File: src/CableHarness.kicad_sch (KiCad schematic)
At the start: 11 parts

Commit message: Update Schematics design
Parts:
- removed J?: MiniFit_2x10_M, Connector_Molex:Molex_Mini-Fit_Jr_5566-20A_2x10_P4.20mm_Vertical, symbol Connector_Generic:Conn_02x10_Counter_Clockwise
- removed J?: MiniFit_2x04_M, Connector_Molex:Molex_Mini-Fit_Jr_5566-08A_2x04_P4.20mm_Vertical, symbol Connector_Generic:Conn_02x04_Counter_Clockwise
- added J13: MiniFit_2x09_F, Connector_Molex:Molex_Mini-Fit_Jr_5566-18A_2x09_P4.20mm_Vertical, symbol Connector_Generic:Conn_02x09_Counter_Clockwise
- added J?: MiniFit_2x05_M, Connector_Molex:Molex_Mini-Fit_Jr_5566-10A_2x05_P4.20mm_Vertical, symbol Connector_Generic:Conn_02x05_Counter_Clockwise
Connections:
- net +5V: now also J13.5 (Pin_5)
- net +BATT: now also J13.1 (Pin_1)
- net ABeam1: now also J13.13 (Pin_13)
- net ABeam2: now also J13.11 (Pin_11)
- net Accessory: now also J?.10 (Pin_10)
- net AuxSwitch1: now also J13.12 (Pin_12)
- net AuxSwitch2: now also J13.10 (Pin_10)
- net BSignal: now also J?.4 (Pin_4)
- net EBlinker: now also J13.6 (Pin_6), J?.5 (Pin_5)
- net GND: no longer J?.4 (Pin_4)
- net HBeam: now also J?.9 (Pin_9)
- net Key: now also J13.7 (Pin_7), J?.1 (Pin_1)
- net Killswitch: now also J13.8 (Pin_8)
- net LBeam: now also J?.8 (Pin_8)
- net LBlinker: now also J?.3 (Pin_3)
- net LowBat: now also J13.9 (Pin_9)
- net PLight: now also J13.14 (Pin_14), J?.7 (Pin_7)
- net RBlinker: now also J?.2 (Pin_2)
- net VInst: now also J13.4 (Pin_4)
- net VLight: now also J13.2 (Pin_2)
- net VRadio: now also J13.3 (Pin_3)
- net GND1 renamed GNDDash
- net GNDDash: now also J13.18 (Pin_18)
- net GND2 renamed GNDEBlinker
- net GNDEBlinker: now also J13.17 (Pin_17)
- net LightSensor: no longer names the net of J?.3 (Pin_3)
- new net GNDRadio: J13.16 (Pin_16), J?.4 (Pin_4)
- no-connect marks 2 -> 5
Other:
- note removed: "Main Board"
- moved on the sheet: J?

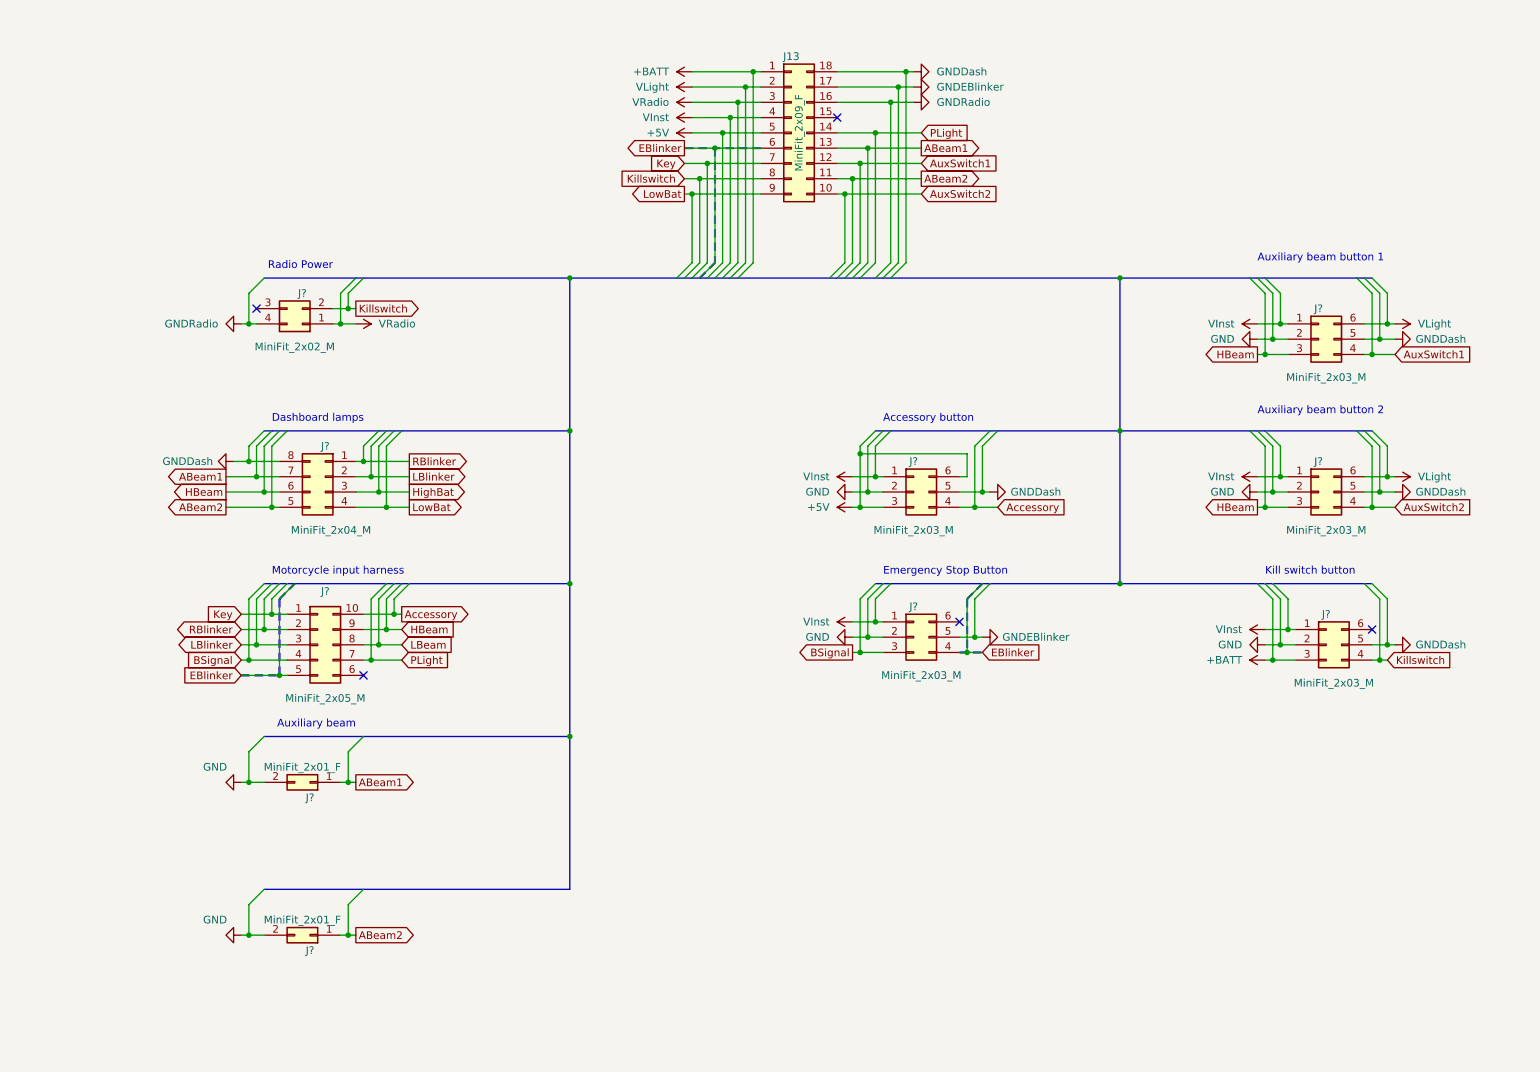
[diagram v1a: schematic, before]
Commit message: Add radio backup battery circuit; Update cable harness; rework main board circuit
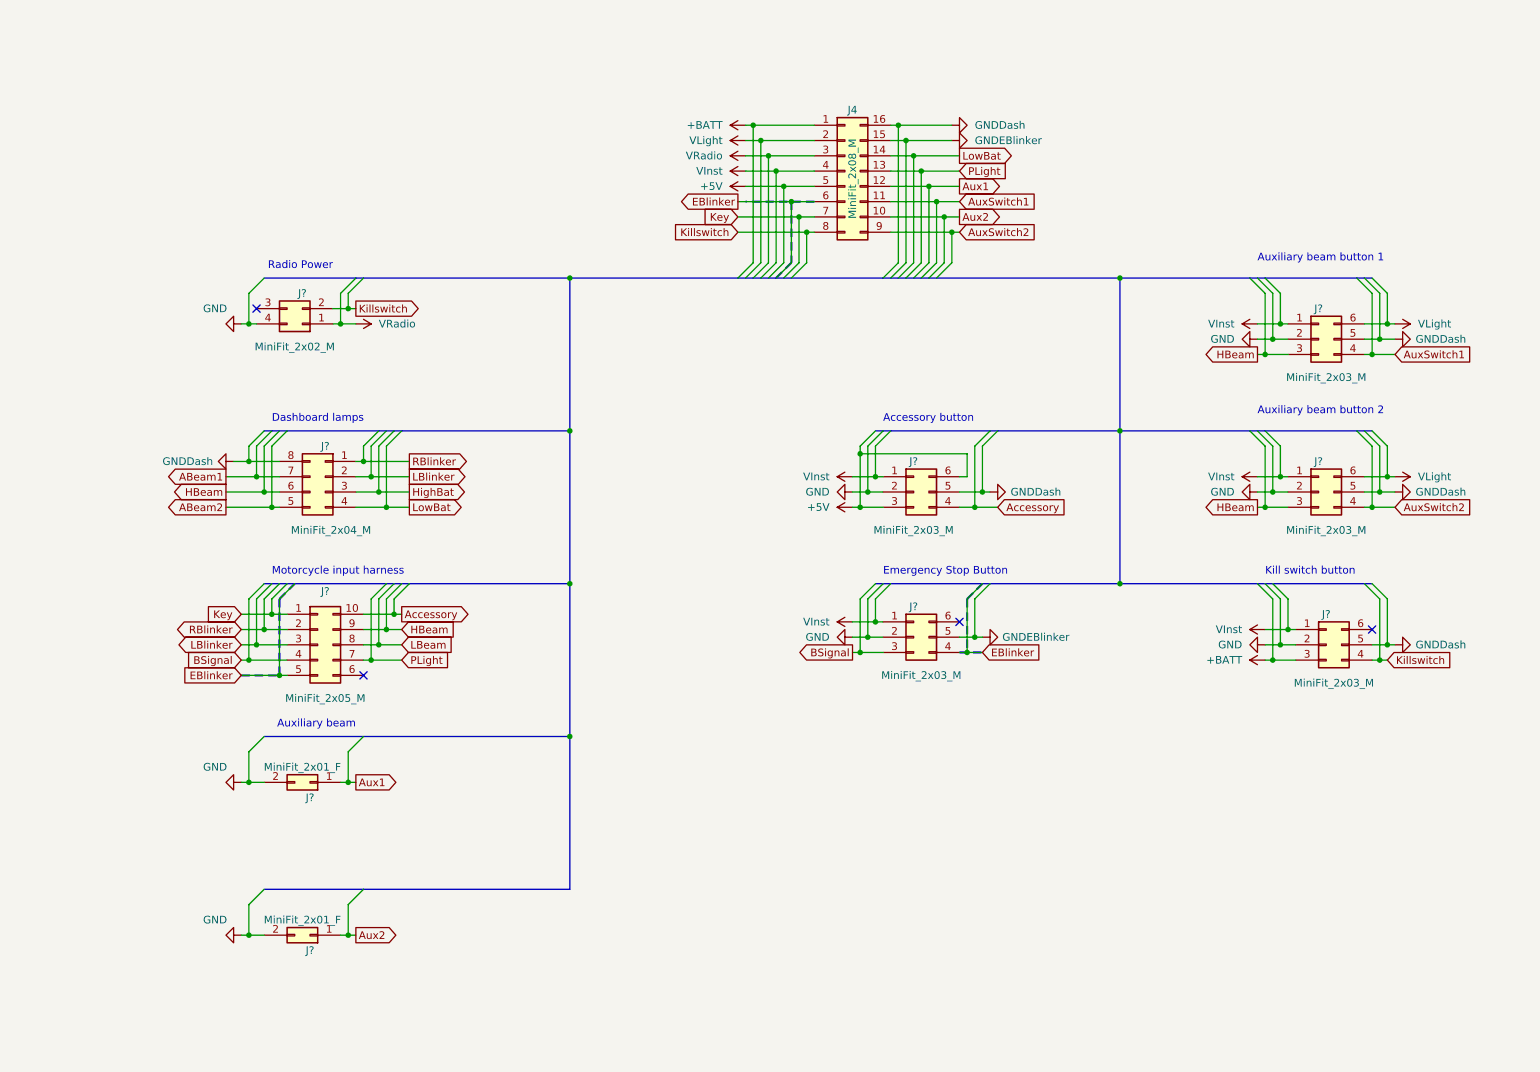
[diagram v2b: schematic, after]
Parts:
- removed J13: MiniFit_2x09_F, Connector_Molex:Molex_Mini-Fit_Jr_5566-18A_2x09_P4.20mm_Vertical, symbol Connector_Generic:Conn_02x09_Counter_Clockwise
- added J4: MiniFit_2x08_M, Connector_Molex:Molex_Mini-Fit_Jr_5566-16A_2x08_P4.20mm_Vertical, symbol Connector_Generic:Conn_02x08_Counter_Clockwise
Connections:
- net GNDRadio is gone; now on net GND: J?.4 (Pin_4)
- net +5V: now also J4.5 (Pin_5)
- net +BATT: now also J4.1 (Pin_1)
- net ABeam1: no longer J?.1 (Pin_1)
- net ABeam2: no longer J?.1 (Pin_1)
- net AuxSwitch1: now also J4.11 (Pin_11)
- net AuxSwitch2: now also J4.9 (Pin_9)
- net EBlinker: now also J4.6 (Pin_6)
- net GNDDash: now also J4.16 (Pin_16)
- net GNDEBlinker: now also J4.15 (Pin_15)
- net Key: now also J4.7 (Pin_7)
- net Killswitch: now also J4.8 (Pin_8)
- net LowBat: now also J4.14 (Pin_14)
- net PLight: now also J4.13 (Pin_13)
- net VInst: now also J4.4 (Pin_4)
- net VLight: now also J4.2 (Pin_2)
- net VRadio: now also J4.3 (Pin_3)
- new net Aux1: J4.12 (Pin_12), J?.1 (Pin_1)
- new net Aux2: J4.10 (Pin_10), J?.1 (Pin_1)
- no-connect marks 5 -> 4

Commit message: update Schematics
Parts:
- removed J4: MiniFit_2x08_M, Connector_Molex:Molex_Mini-Fit_Jr_5566-16A_2x08_P4.20mm_Vertical, symbol Connector_Generic:Conn_02x08_Counter_Clockwise
- removed J? (x4): MiniFit_2x03_M, Connector_Molex:Molex_Mini-Fit_Jr_5566-06A_2x03_P4.20mm_Vertical, symbol Connector_Generic:Conn_02x03_Counter_Clockwise
- removed J?: MiniFit_2x01_F, Connector_Molex:Molex_Mini-Fit_Jr_5566-02A_2x01_P4.20mm_Vertical, symbol Connector_Generic:Conn_02x01
- removed J?: MiniFit_2x05_M, Connector_Molex:Molex_Mini-Fit_Jr_5566-10A_2x05_P4.20mm_Vertical, symbol Connector_Generic:Conn_02x05_Counter_Clockwise
- removed J?: MiniFit_2x04_M, Connector_Molex:Molex_Mini-Fit_Jr_5566-08A_2x04_P4.20mm_Vertical, symbol Connector_Generic:Conn_02x04_Counter_Clockwise
- added J52: Car Socket, symbol Connector:Conn_Coaxial
- added J69: 1217080-1, 1217080-1, symbol SamacSys_Parts:1217080-1
- added J?: MiniFit_2x10_M, symbol Connector_Generic:Conn_02x10_Counter_Clockwise
- added J?: MiniFit_2x04_M, Connector_Molex:Molex_Mini-Fit_Jr_5566-08A_2x04_P4.20mm_Vertical, symbol Connector_Generic:Conn_02x04_Counter_Clockwise
- added J? (x2): Barrel_Jack, Connector_BarrelJack:BarrelJack_CUI_PJ-063AH_Horizontal, symbol Connector:Barrel_Jack
- added J?: MiniFit_2x01_F, Connector_Molex:Molex_Mini-Fit_Jr_5566-02A_2x01_P4.20mm_Vertical, symbol Connector_Generic:Conn_02x01
- added J? (x4): MiniFit_2x03_M, Connector_Molex:Molex_Mini-Fit_Jr_5566-06A_2x03_P4.20mm_Vertical, symbol Connector_Generic:Conn_02x03_Counter_Clockwise
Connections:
- net GNDEBlinker is gone; now on net GNDDash: J?.5 (Pin_5)
- net Killswitch is gone; now on net Key: J?.2 (Pin_2)
- net +5V: now also J?.3 (Pin_3), J?.5 (Pin_5)
- net +BATT: now also J?.6 (Pin_6)
- net Accessory: now also J?.1 (Pin_1), J?.4 (Pin_4)
- net GND: now also J52.2 (Ext), J69.1, J69.2, J?.2, J?.2, J?.2 (Pin_2), J?.2 (Pin_2), J?.2 (Pin_2), J?.2 (Pin_2)
- net GNDDash: now also J?.5 (Pin_5), J?.5 (Pin_5), J?.5 (Pin_5), J?.6 (Pin_6), J?.7 (Pin_7)
- net HBeam: now also J?.14 (Pin_14), J?.2 (Pin_2), J?.5 (Pin_5)
- net Key: now also J?.10 (Pin_10), J?.8 (Pin_8)
- net LBeam: now also J?.12 (Pin_12), J?.3 (Pin_3)
- net LBlinker: now also J?.19 (Pin_19), J?.2 (Pin_2), J?.6 (Pin_6)
- net PLight: now also J?.9 (Pin_9)
- net RBlinker: now also J?.1 (Pin_1), J?.20 (Pin_20), J?.7 (Pin_7)
- net VInst: now also J?.1 (Pin_1), J?.1 (Pin_1), J?.1 (Pin_1), J?.2 (Pin_2), J?.6 (Pin_6); no longer J?.1 (Pin_1)
- net VLight: now also J?.3 (Pin_3), J?.4 (Pin_4)
- net VRadio: now also J?.1 (Pin_1)
- net Aux1 renamed AuxHBeam
- net AuxHBeam: now also J?.13 (Pin_13)
- net BSignal renamed SignalRelay
- net SignalRelay: now also J?.5 (Pin_5)
- net EBlinker renamed Hazard
- net Hazard: now also J?.18 (Pin_18)
- new net AuxBeams: J?.15 (Pin_15), J?.4 (Pin_4)
- new net AuxLBeam: J?.1 (Pin_1), J?.11 (Pin_11)
- new net AuxSwitch: J?.16 (Pin_16), J?.4 (Pin_4)
- new net HazardLed: J?.1 (Pin_1), J?.17 (Pin_17), J?.3 (Pin_3)
- new net VOutlet: J?.3 (Pin_3), J?.3 (Pin_3)
- new net VOutlet_Jack: J52.1 (In), J?.1, J?.1, J?.4 (Pin_4)
- no-connect marks 4 -> 6
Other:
- note added: "Auxiliary Beams Buttons"
- note added: "Auxiliary High Beam"
- note added: "Auxiliary Low beam"
- note added: "Car Socket"
- note added: "Car Socket Button"
- note added: "Common Ground"
- note added: "Main Board"
- note removed: "Auxiliary beam"
- note removed: "Auxiliary beam button 1"
- note removed: "Auxiliary beam button 2"
- note removed: "Kill switch button"
- moved on the sheet: J?

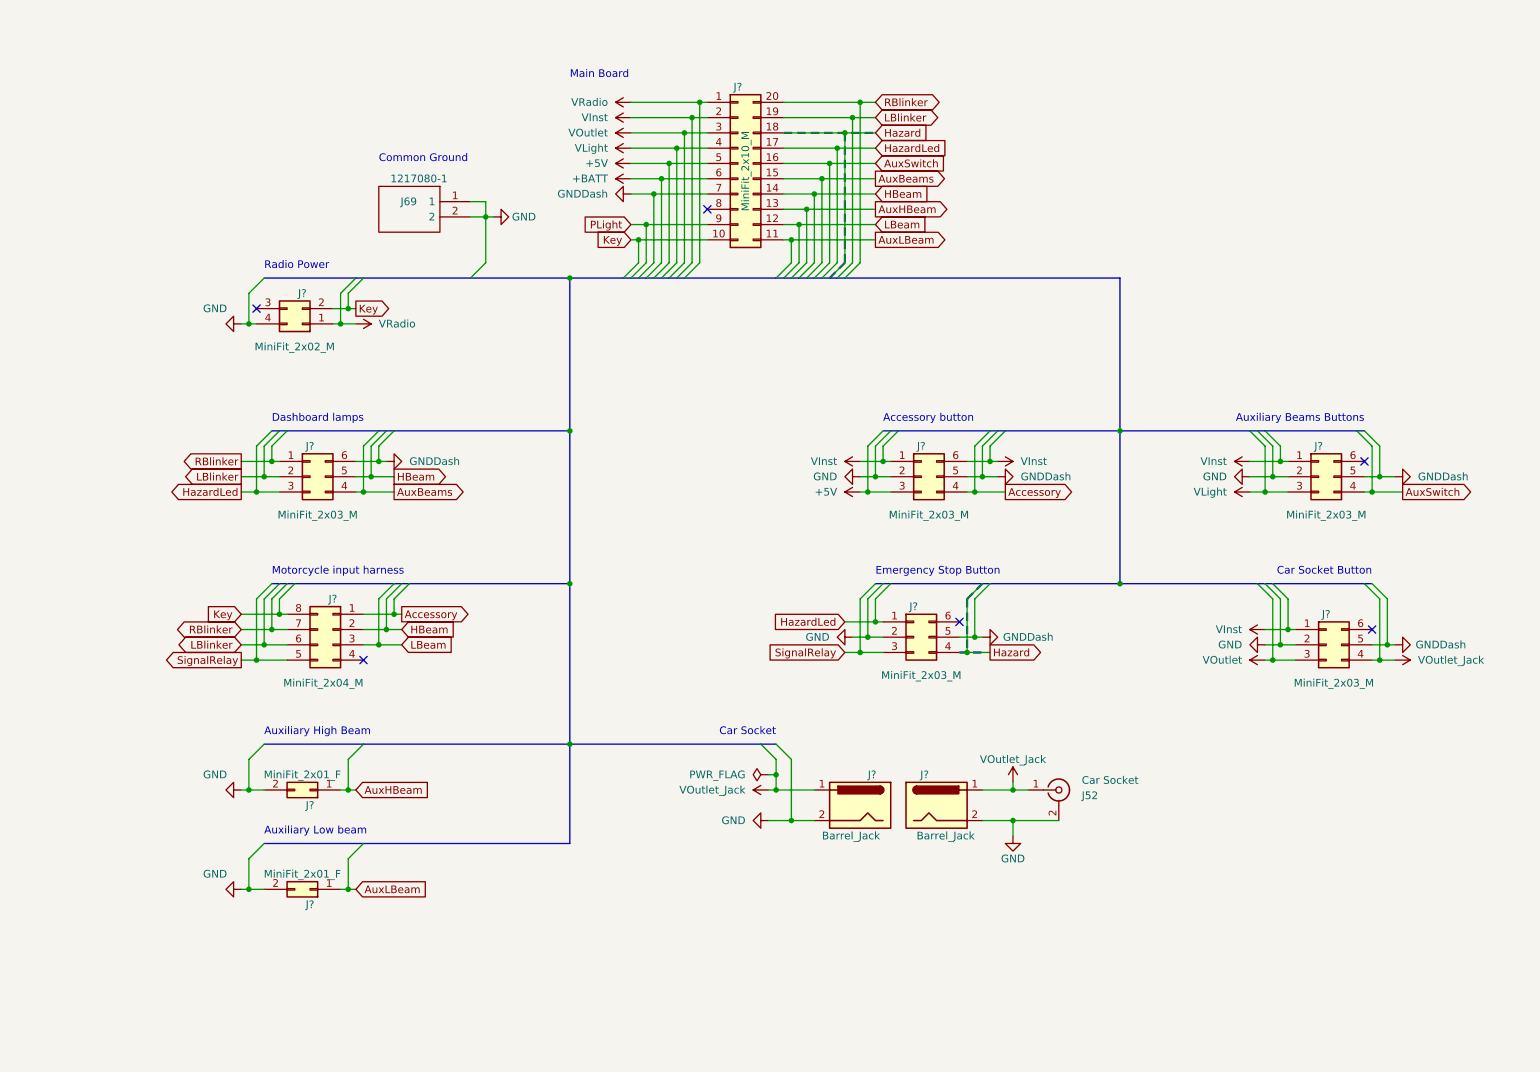
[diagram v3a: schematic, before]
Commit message: Update Schmatics; Cleanup unecessary circuits; Simplify blinkers dimmers; Update PCB; Colorize motorcycle electric diagram.
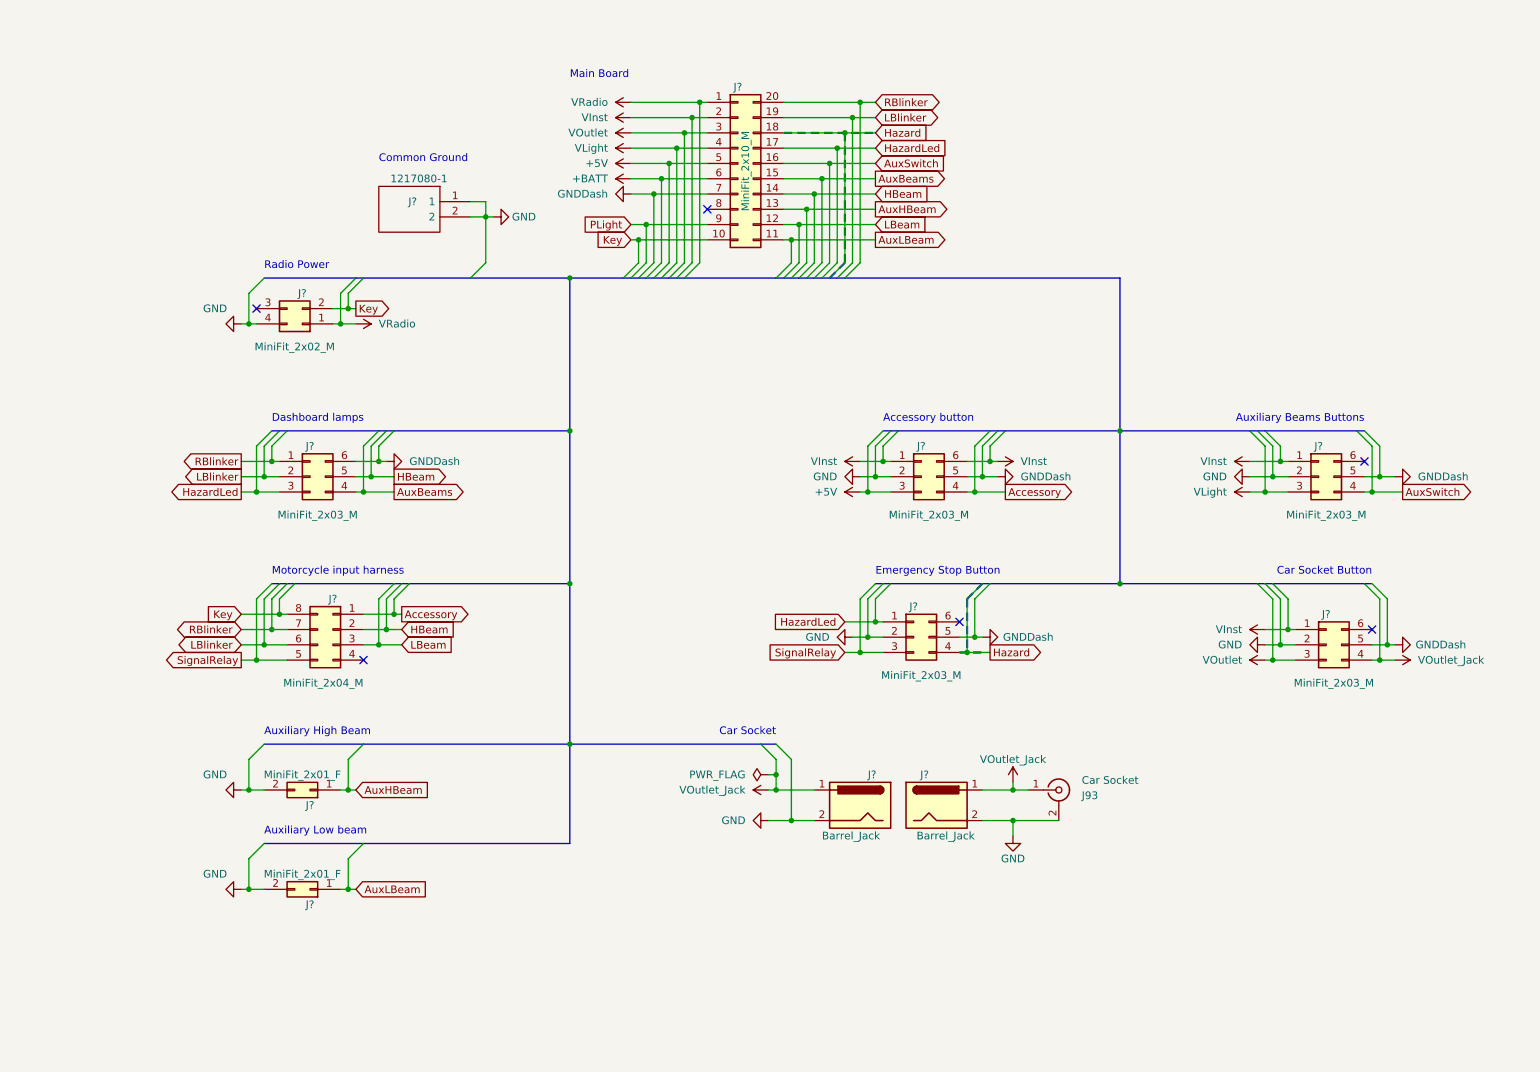
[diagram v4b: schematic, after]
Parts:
- renumbered J52 to J93, J69 to J?
